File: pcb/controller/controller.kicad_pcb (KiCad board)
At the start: 2 copper layers, 54 x 10 mm, 43 parts, among them J1 Conn_01x01, J2 Conn_01x02, J3 Conn_01x03, J4 Conn_02x02_Odd_Even, Q1 RU1C001ZPTL, Q2 CSD25481F4T, Q3 BC847BLT1G, U1 TPS613222ADBVR, U2 LIS2DE12TR, U3 MSP430FR2512IRHLR, U4 BMG250, Y1 32.786kHz

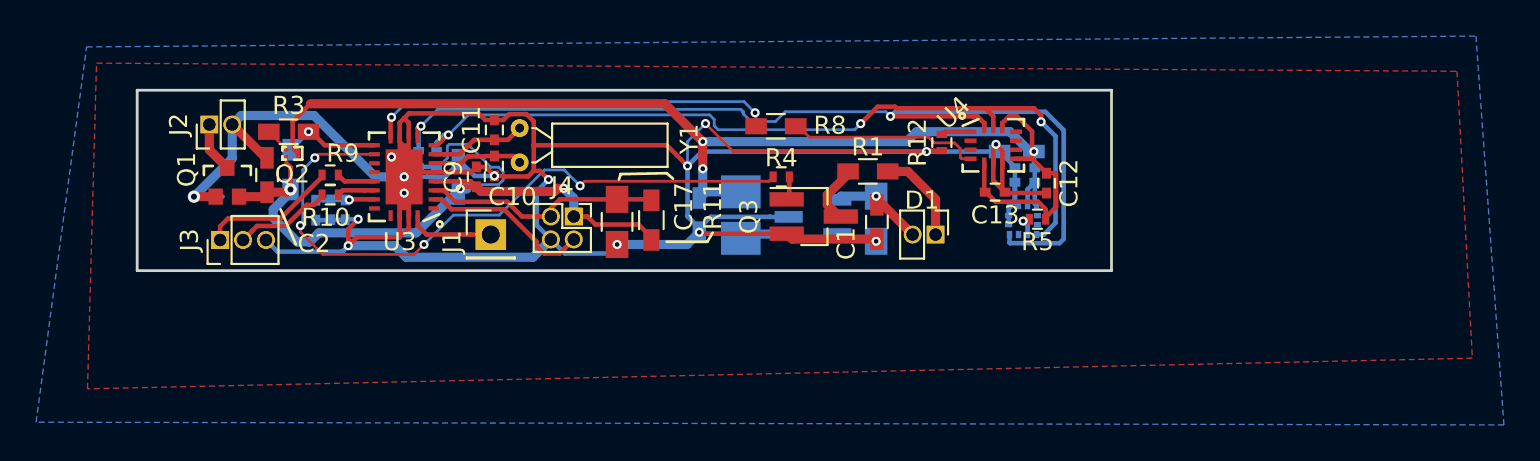
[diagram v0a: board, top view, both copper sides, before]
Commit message: Resize vias
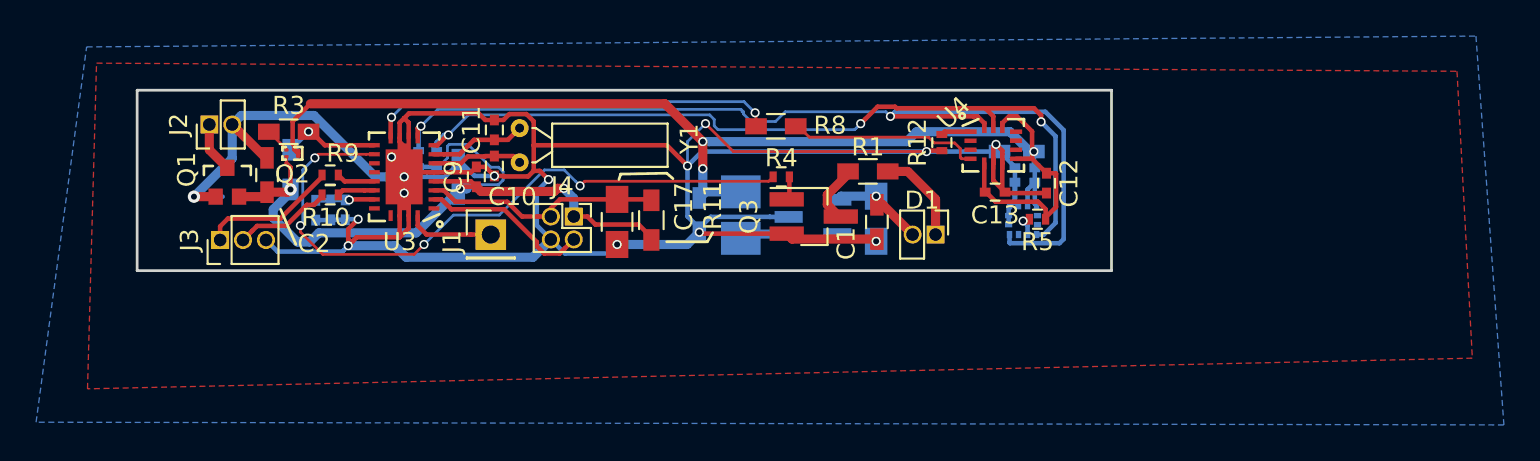
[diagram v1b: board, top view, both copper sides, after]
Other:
- rule via_min_drill: 0.254 -> 0.3302

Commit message: Small changes/add receiver zip
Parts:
- R1: value 1k -> 33
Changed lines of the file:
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@@
-(kicad_pcb (version 20171130) (host pcbnew 5.0.0)
+(kicad_pcb (version 20171130) (host pcbnew 5.0.1)
   (general
     (thickness 1.6)
@@
       (effects (font (size 1 1) (thickness 0.15)))
     )
-    (fp_text value 1k (at 0 1.55 180) (layer F.Fab)
-      (effects (font (size 1 1) (thickness 0.15)))
-    )
+    (fp_text value 33 (at 0 1.55 180) (layer F.Fab)
+      (effects (font (size 1 1) (thickness 0.15)))
+    )
